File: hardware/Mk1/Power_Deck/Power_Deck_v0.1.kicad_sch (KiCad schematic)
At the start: 4 parts, among them J1 XT30_IN, J2 INA219_MODULE, J3 MP1584_MODULE, SW1 SW_SPST

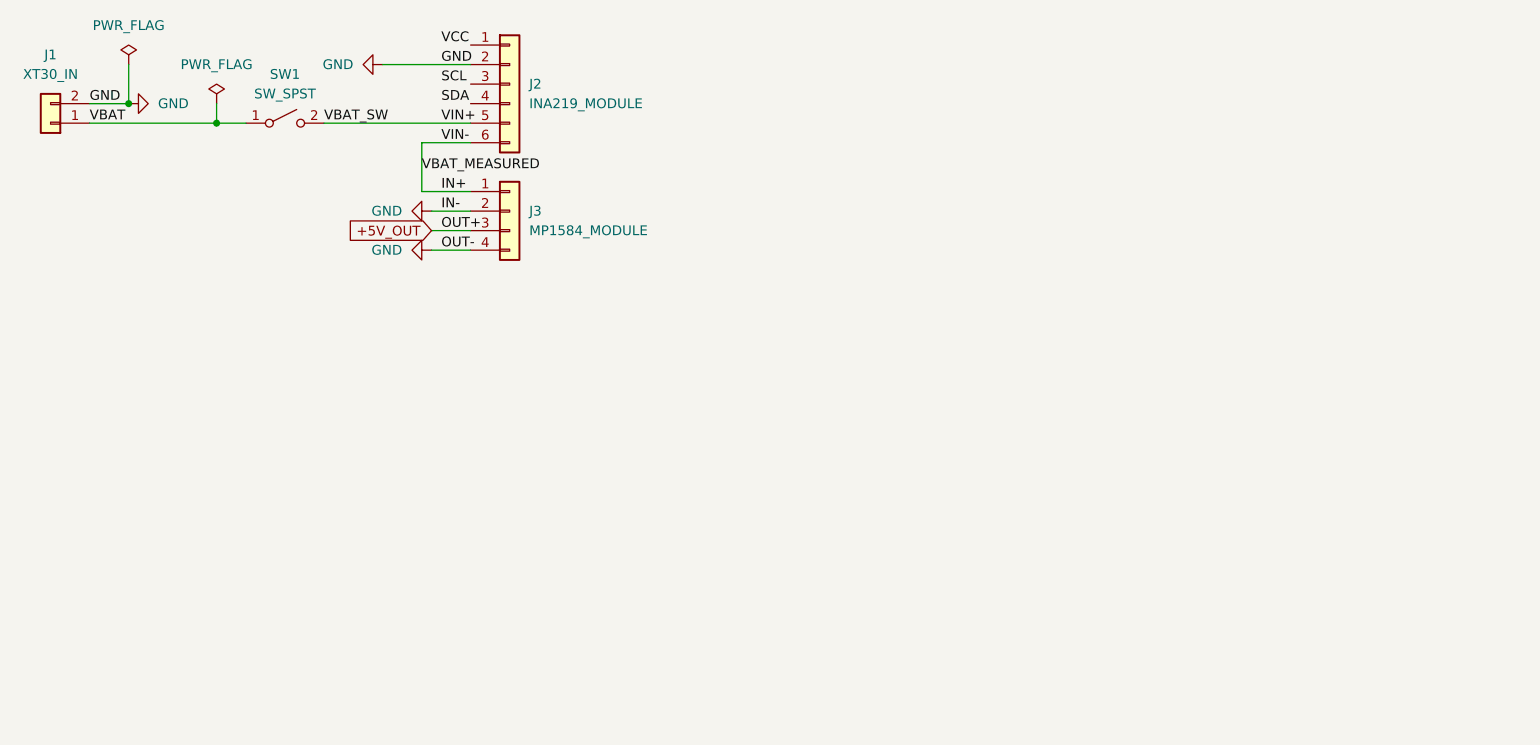
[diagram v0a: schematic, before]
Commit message: feat(power-deck): complete v0.1 schematic
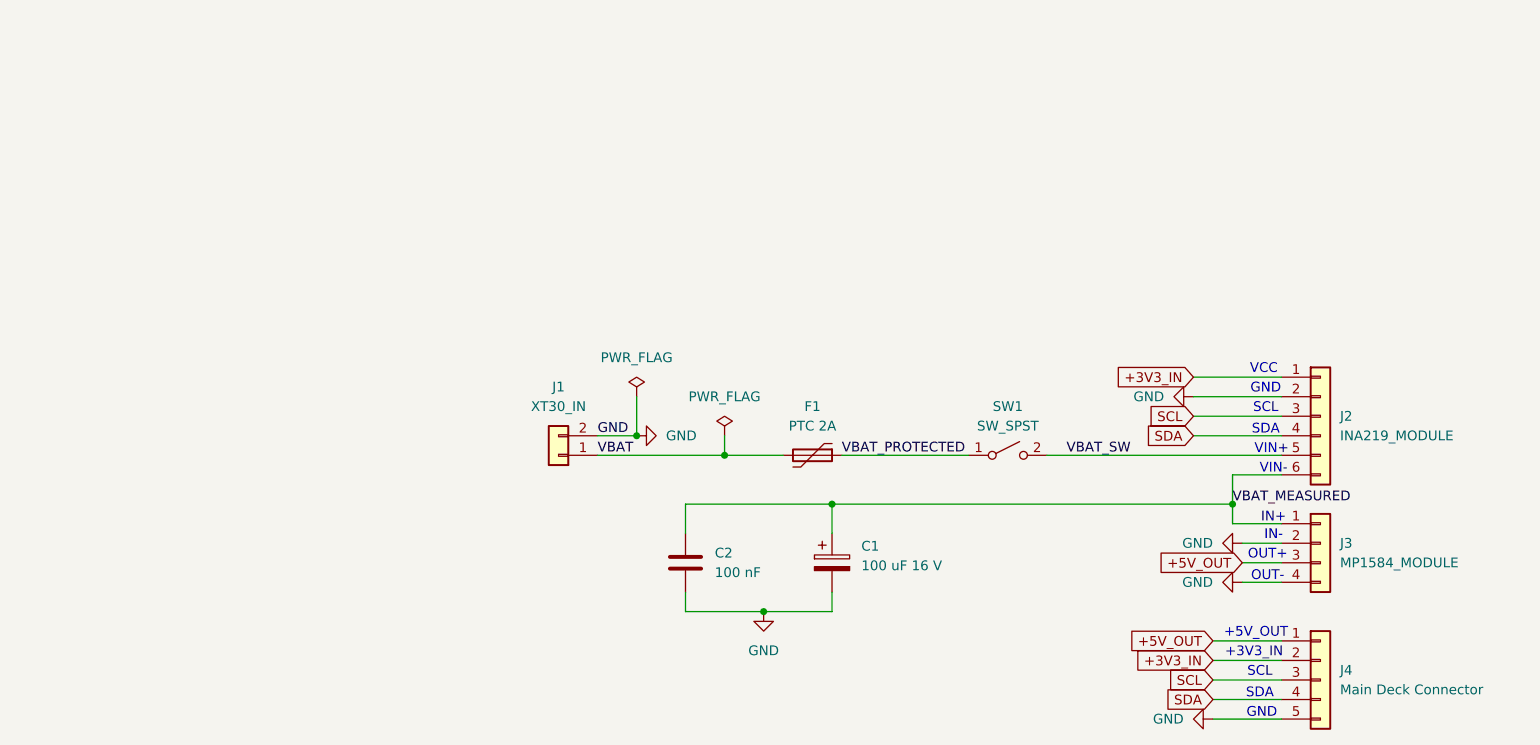
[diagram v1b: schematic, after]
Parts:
- added C1: 100 uF 16 V, symbol Device:C_Polarized
- added C2: 100 nF, symbol Device:C
- added F1: PTC 2A, symbol Device:Polyfuse
- added J4: Main Deck Connector, symbol Connector_Generic:Conn_01x05
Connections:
- net +5V_OUT: now also J4.1 (Pin_1)
- net GND: now also C1.2, C2.2, J4.5 (Pin_5)
- net SCL: now also J2.3 (Pin_3), J4.3 (Pin_3)
- net SDA: now also J2.4 (Pin_4), J4.4 (Pin_4)
- net VBAT: now also F1.2; no longer SW1.1 (A)
- net +3V3_IN: now reaches J2.1 (Pin_1)
- net +3V3_IN: now also J4.2 (Pin_2)
- net IN+ renamed VBAT_MEASURED
- net VBAT_MEASURED: now also C1.1, C2.1
- new net VBAT_PROTECTED: F1.1, SW1.1 (A)
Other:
- note added: "+3V3_IN"
- note added: "+5V_OUT"
- note added: "GND"
- note added: "IN+"
- note added: "IN-"
- note added: "OUT+"
- note added: "OUT-"
- note added: "SCL"
- note added: "SDA"
- note added: "VCC"
- note added: "VIN+"
- note added: "VIN-"
- title: (none) -> Power Deck
- moved on the sheet: J1, J2, J3, SW1
